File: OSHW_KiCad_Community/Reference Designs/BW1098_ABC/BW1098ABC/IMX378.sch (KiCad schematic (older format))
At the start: 11 parts

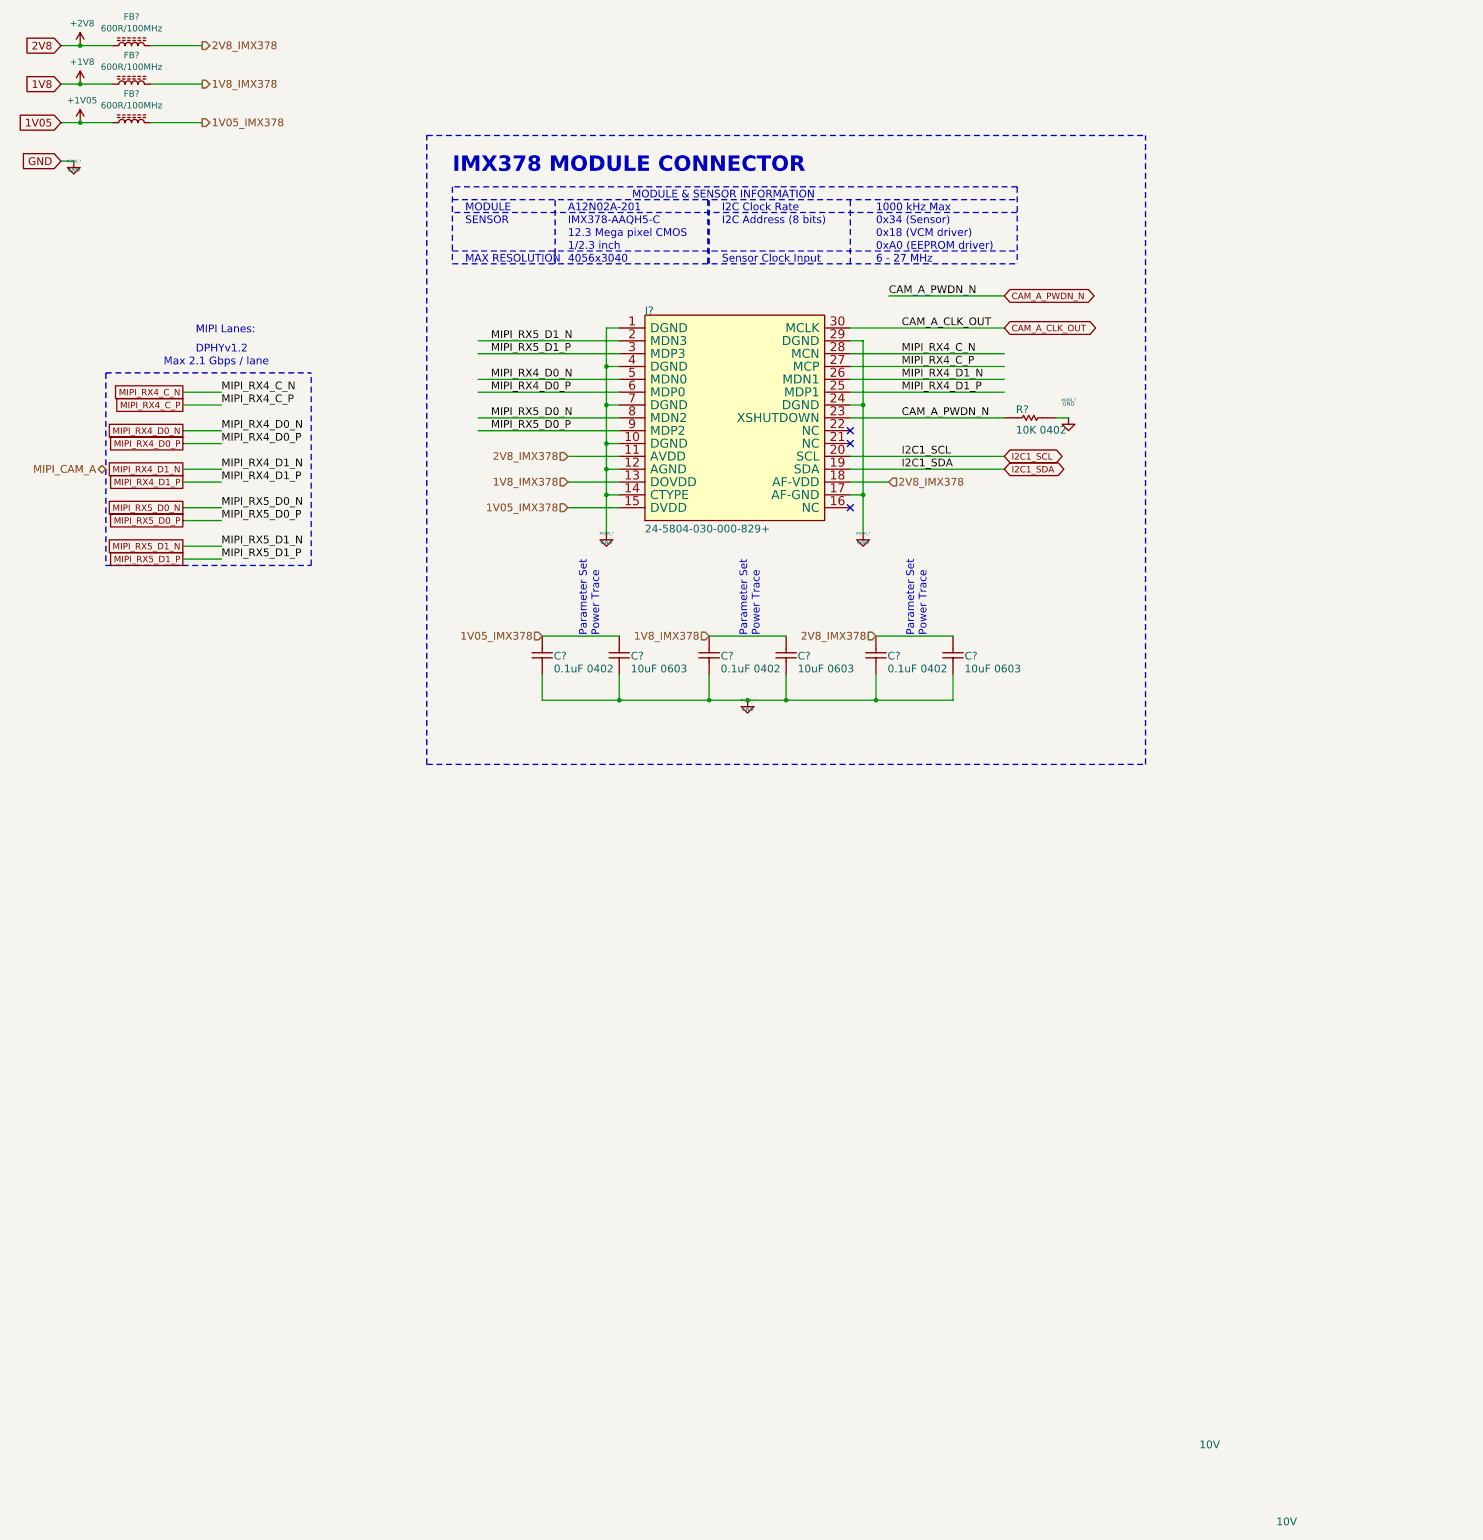
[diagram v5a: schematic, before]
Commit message: added busses, fixed hierarchical labeling, just need to fix an erc thing with my buses then itll pass
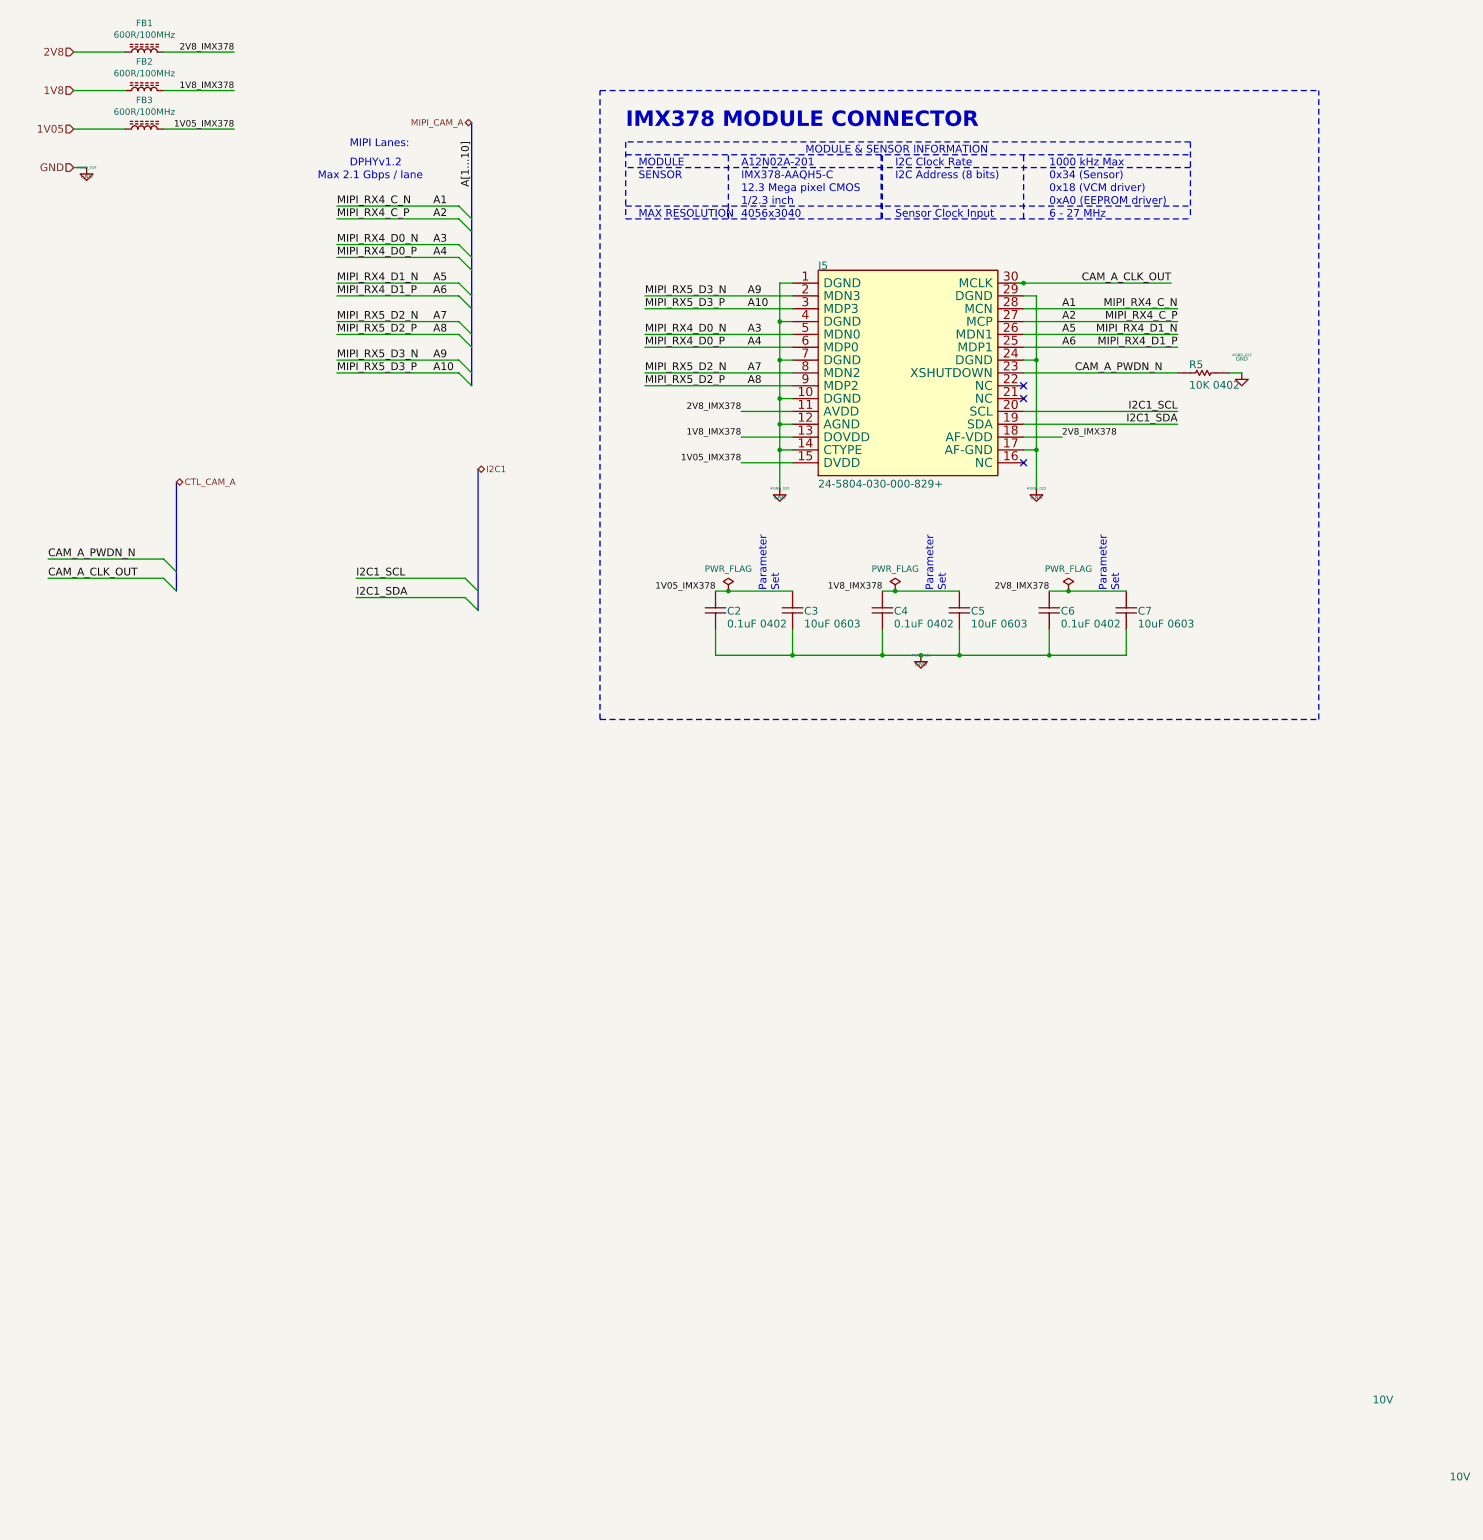
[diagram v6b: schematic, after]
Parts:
- gave numbers to parts that had none: 11
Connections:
- net labels added: A1, A10, A2, A3, A4, A5, A6, A7, A8, A9, A[1...10], CTL_CAM_A, I2C1, MIPI_RX5_D2_N, MIPI_RX5_D2_P, MIPI_RX5_D3_N, MIPI_RX5_D3_P
- net labels removed: +1V05, +1V8, +2V8, MIPI_RX5_D0_N, MIPI_RX5_D0_P, MIPI_RX5_D1_N, MIPI_RX5_D1_P
- wire segments 73 -> 77
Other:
- note added: "Parameter \nSet\n"
- note removed: "Parameter Set\nPower Trace"
- moved on the sheet: C2, C3, C4, C5, C6, C7, FB1, FB2, FB3, J5, R5
